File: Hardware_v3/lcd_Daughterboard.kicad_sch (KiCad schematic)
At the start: 5 parts, among them J3 Conn_01x03_Pin, J4 Conn_01x03_Pin, J5 Conn_01x02_Pin, J6 Conn_01x02_Pin, U1 ILI9341_SPI_Bare

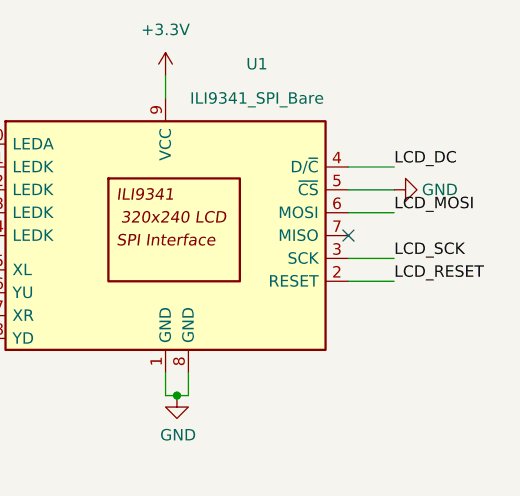
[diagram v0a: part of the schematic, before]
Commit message: V3 production files submitted to JLC
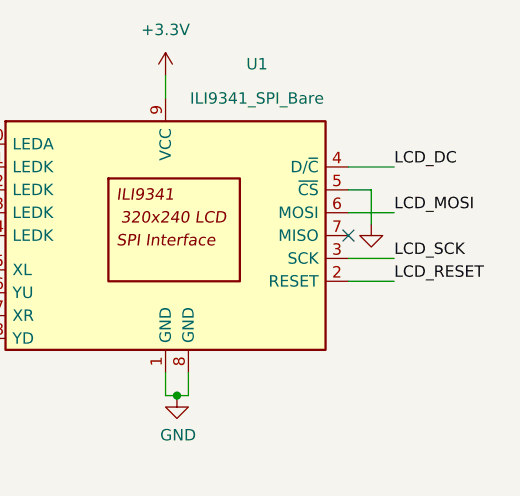
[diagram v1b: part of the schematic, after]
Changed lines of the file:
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@@
-	(wire
-		(pts
-			(xy 147.32 36.83) (xy 152.4 36.83)
-		)
-		(stroke
-			(width 0)
-			(type default)
-		)
-	)
 	(wire
 		(pts
@@
 	(wire
 		(pts
+			(xy 149.86 40.64) (xy 149.86 36.83)
+		)
+		(stroke
+			(width 0)
+			(type default)
+		)
+	)
+	(wire
+		(pts
 			(xy 147.32 46.99) (xy 152.4 46.99)
 		)
@@
 		(pts
 			(xy 127 57.15) (xy 127 59.69)
+		)
+		(stroke
+			(width 0)
+			(type default)
+		)
+	)
+	(wire
+		(pts
+			(xy 149.86 36.83) (xy 147.32 36.83)
 		)
 		(stroke
@@
 	(symbol
 		(lib_id "power:GND")
-		(at 152.4 36.83 90)
+		(at 149.86 40.64 0)
 		(unit 1)
 		(exclude_from_sim no)
@@
 		(dnp no)
 		(property "Reference" "#PWR09"
-			(at 158.75 36.83 0)
+			(at 149.86 46.99 0)
 			(effects
 				(font
@@
 		)
 		(property "Value" "GND"
-			(at 157.48 36.83 90)
-			(effects
-				(font
-					(size 1.27 1.27)
-				)
+			(at 150.622 45.72 90)
+			(effects
+				(font
+					(size 1.27 1.27)
+				)
+				(hide yes)
 			)
 		)
 		(property "Footprint" ""
-			(at 152.4 36.83 0)
+			(at 149.86 40.64 0)
 			(effects
 				(font
@@
 		)
 		(property "Datasheet" ""
-			(at 152.4 36.83 0)
+			(at 149.86 40.64 0)
 			(effects
 				(font
@@
 		)
 		(property "Description" "Power symbol creates a global label with name \"GND\" , ground"
-			(at 152.4 36.83 0)
-			(effects
-				(font
+			(at 149.86 40.64 0)
+			(effects
+				(font
